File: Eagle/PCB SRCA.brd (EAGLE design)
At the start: 160 x 100 mm, 75 parts, among them IC1 DSPIC30F4011-30I_P, IC2 LM324LVIDR, IC3 LMT86QDCKRQ1, IC4 LORA_MOTE, IC5 FT232RL-REEL, J1 TBL002A-350-03GR-2OR, J2 TBL002A-350-03GR-2OR, J3 TBL002A-350-03GR-2OR, J4 44914-0801, J5 ICSP, J6 TBL002A-350-03GR-2OR, J7 44914-0401, Q1 TIP41C, T1 2N3904, T12 2N3904, T13 2N3904, T2 2N3904, T3 2N3904, T4 2N3904, T5 2N3904, T6 2N3904, T7 2N3904

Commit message: 12/08/2021
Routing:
- net MCLR: track 126.5 -> 129.0 mm
- net GATE_DOWN: track 42.1 -> 43.7 mm
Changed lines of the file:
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@@
 <wire x1="44.704" y1="60.5632" x2="44.704" y2="61.5696" width="0.254" layer="16"/>
 <wire x1="44.288" y1="60.1472" x2="44.704" y2="60.5632" width="0.254" layer="16"/>
-<wire x1="7.112" y1="60.1472" x2="28.4" y2="60.1472" width="0.254" layer="16"/>
-<wire x1="28.4" y1="60.1472" x2="44.288" y2="60.1472" width="0.254" layer="16"/>
+<wire x1="7.112" y1="60.1472" x2="31.0352" y2="60.1472" width="0.254" layer="16"/>
+<wire x1="31.0352" y1="60.1472" x2="44.288" y2="60.1472" width="0.254" layer="16"/>
 <wire x1="5.4864" y1="61.7728" x2="7.112" y2="60.1472" width="0.254" layer="16"/>
 <wire x1="79.0448" y1="61.7728" x2="79.21" y2="61.575" width="0.254" layer="1"/>
 <wire x1="5.4864" y1="61.7728" x2="5.34" y2="61.82" width="0.254" layer="16"/>
-<wire x1="8.5344" y1="28.628" x2="8.5344" y2="27.2288" width="0.254" layer="1"/>
-<wire x1="11.7352" y1="31.864" x2="11.7352" y2="31.8288" width="0.254" layer="1"/>
-<wire x1="11.7352" y1="31.8288" x2="8.5344" y2="28.628" width="0.254" layer="1"/>
-<wire x1="11.6352" y1="43.3824" x2="11.6352" y2="31.964" width="0.254" layer="16"/>
-<wire x1="11.6352" y1="31.964" x2="11.7352" y2="31.864" width="0.254" layer="16"/>
-<wire x1="8.5344" y1="27.2288" x2="8.43" y2="27.07" width="0.254" layer="1"/>
+<wire x1="12.3344" y1="40.928" x2="12.3344" y2="33.008878125" width="0.254" layer="1"/>
+<wire x1="31.1352" y1="56.664" x2="28.0704" y2="56.664" width="0.254" layer="1"/>
+<wire x1="28.0704" y1="56.664" x2="12.3344" y2="40.928" width="0.254" layer="1"/>
+<wire x1="31.0352" y1="60.1472" x2="31.0352" y2="56.764" width="0.254" layer="16"/>
+<wire x1="31.0352" y1="56.764" x2="31.1352" y2="56.664" width="0.254" layer="16"/>
+<wire x1="12.3344" y1="33.008878125" x2="8.43" y2="27.07" width="0.254" layer="1"/>
 <via x="78.6384" y="64.6176" extent="1-16" drill="0.35"/>
-<via x="11.7352" y="31.864" extent="1-16" drill="0.35"/>
-<wire x1="11.6352" y1="43.3824" x2="28.4" y2="60.1472" width="0.254" layer="16"/>
+<via x="31.1352" y="56.664" extent="1-16" drill="0.35"/>
 </signal>
 <signal name="POT_LINEAR">
@@
 <contactref element="IC1" pad="19"/>
 <wire x1="7.9726" y1="35.4174" x2="8.29" y2="35.1" width="0.254" layer="1"/>
-<wire x1="33.49" y1="61.575" x2="33.49" y2="60.9348" width="0.254" layer="1"/>
-<wire x1="33.49" y1="60.9348" x2="7.9726" y2="35.4174" width="0.254" layer="1"/>
 <wire x1="7.9726" y1="35.4174" x2="7.9184" y2="35.3632" width="0.254" layer="1"/>
 <wire x1="8.29" y1="35.1" x2="5.41" y2="35.1" width="0.254" layer="1"/>
 <wire x1="5.41" y1="35.1" x2="4.11" y2="36.4" width="0.254" layer="1"/>
+<wire x1="33.49" y1="61.575" x2="29.615" y2="57.7" width="0.254" layer="1"/>
+<wire x1="29.615" y1="57.7" x2="27.2" y2="57.7" width="0.254" layer="1"/>
+<wire x1="27.2" y1="57.7" x2="11.4" y2="41.9" width="0.254" layer="1"/>
+<wire x1="11.4" y1="38.21" x2="8.29" y2="35.1" width="0.254" layer="1"/>
+<wire x1="11.4" y1="41.9" x2="11.4" y2="38.21" width="0.254" layer="1"/>
 </signal>
 <signal name="AVAILABLE">

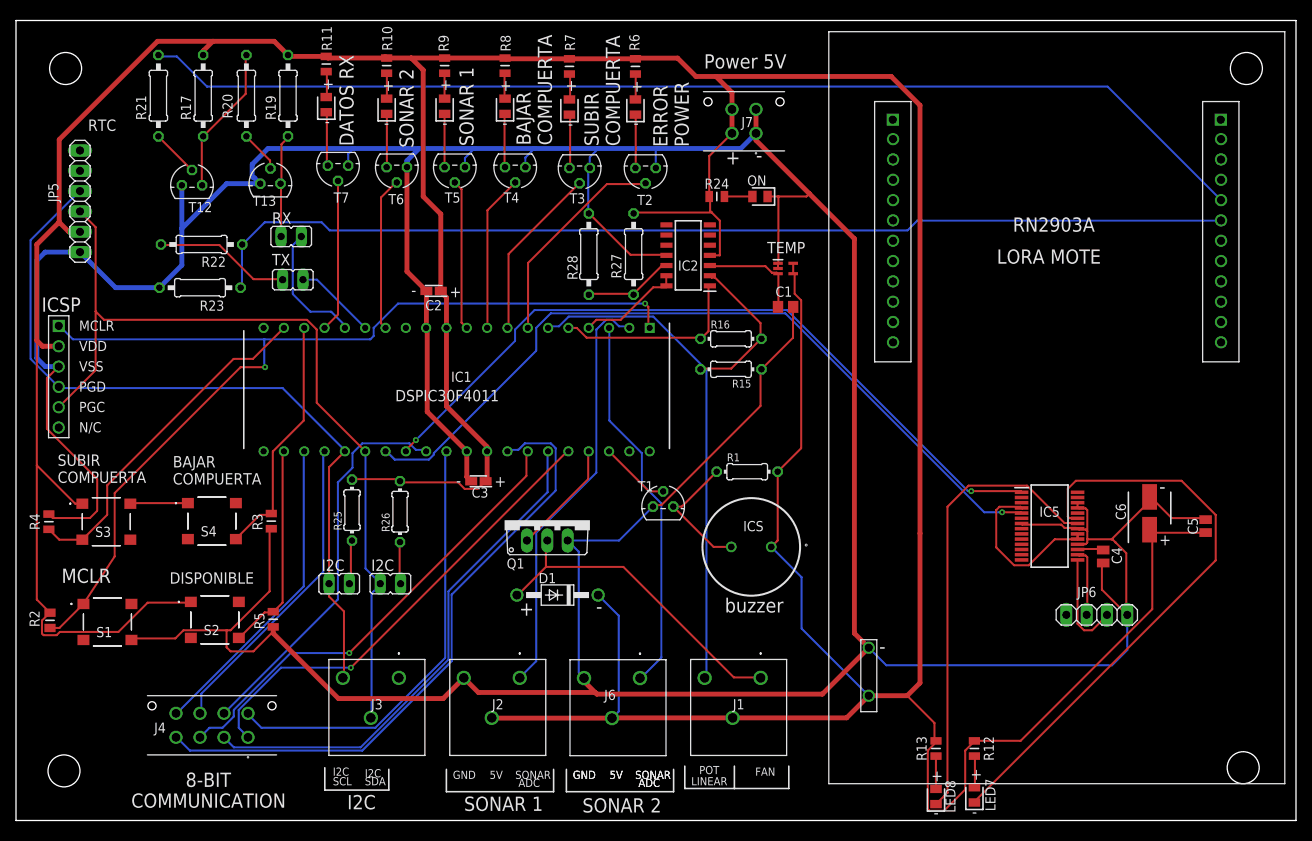
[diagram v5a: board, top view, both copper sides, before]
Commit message: 20/08/2021
se adjunta los archivos de la PCB  final con logo  y archivo gerber
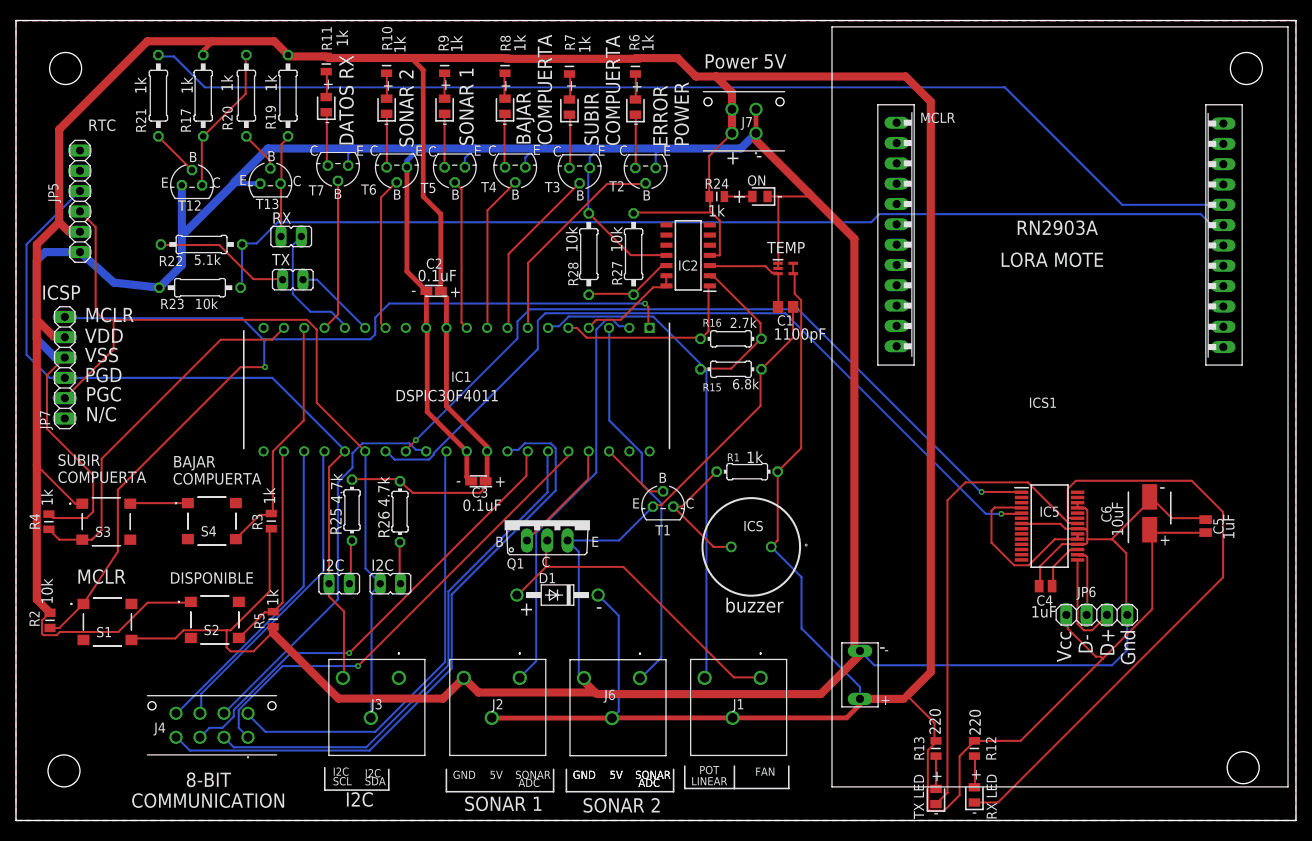
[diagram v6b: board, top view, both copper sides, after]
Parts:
- removed IC4: LORA_MOTE, LORA_MOTE:LORA_MOTE_RN2903
- removed J5: ICSP, ICSP:ICSP
- added ICS1: LORA_MOTE, LORA_MOTE:LORA_MOTE_RN2903
- added JP7: (no value), pinhead:1X06
- moved C4 8.10 mm to (128.7, 29.3), turned to 0 degrees
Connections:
- removed net N$19: JP6.1
- net GND: now also ICS1.GND, JP7.4; no longer IC4.GND, J5.VSS
- net I2C_SCL: now also JP7.3; no longer J5.PGD
- net I2C_SDA: now also JP7.2; no longer J5.PGC
- net MCLR: now also JP7.6; no longer J5.MCLR
- net RX_LORA: now also ICS1.UARTTX; no longer IC4.UARTTX
- net TX_LORA: now also ICS1.UARTRX; no longer IC4.UARTRX
- net V+: now also ICS1.V5, JP6.1, JP7.5; no longer IC4.V5, J5.VDD
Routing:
- net V+: track 608.9 -> 622.2 mm
- net N$20: track 3.28 -> 6.66 mm
- net N$15: track 74.2 -> 77.4 mm
- net GATE_DOWN: track 43.7 -> 46.7 mm
- net I2C_SDA: track 108.0 -> 106.5 mm
- net N$18: track 57.2 -> 58.0 mm
- net TX_LORA: track 140.4 -> 141.1 mm
- net BIT_5: track 55.1 -> 55.8 mm
- net BIT_4: track 78.5 -> 79.0 mm
- net N$14: track 21.7 -> 22.2 mm
- net MCLR: track 129.0 -> 129.5 mm
- added copper zone on layer 1, net GND
- added copper zone on layer 16, net GND
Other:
- board text added: "0.1uF"
- board text added: "10k"
- board text added: "10uF"
- board text added: "1100pF"
- board text added: "1k"
- board text added: "1uF"
- board text added: "2.7k"
- board text added: "220"
- board text added: "4.7k"
- board text added: "5.1k"
- board text added: "6.8k"
- board text added: "B"
- board text added: "C"
- board text added: "C:/Users/ASUS/Desktop/nombe.bmp"
- board text added: "D+"
- board text added: "D-"
- board text added: "E"
- board text added: "N/C"
- board text added: "PGC"
- board text added: "PGD"
- board text added: "RX LED"
- board text added: "TX LED"
- board text added: "VDD"
- board text added: "VSS"

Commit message: 23-08-2021
actualizaciones de nombres y logos
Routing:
- net BIT_6: track 49.4 -> 50.6 mm
- net UART_TX_2: track 100.1 -> 101.3 mm
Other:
- board text added: "FT232"
- board text added: "RTC DS3231"
- board text removed: "C:/Users/ASUS/Desktop/nombe.bmp"
- board text removed: "RTC"
